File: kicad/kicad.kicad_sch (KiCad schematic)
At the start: 7 parts, among them J1 Screw_Terminal_01x14, U1 Pico

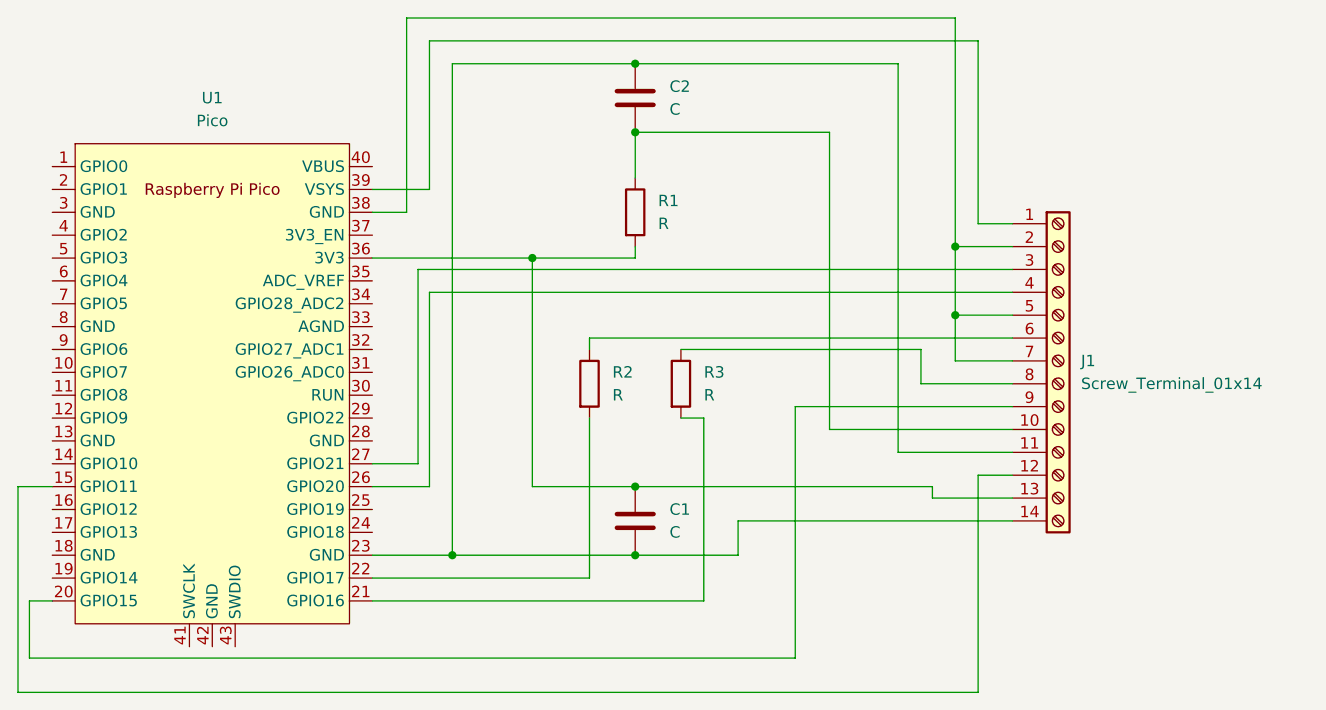
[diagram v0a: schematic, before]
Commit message: added kicad board that I'm getting printed
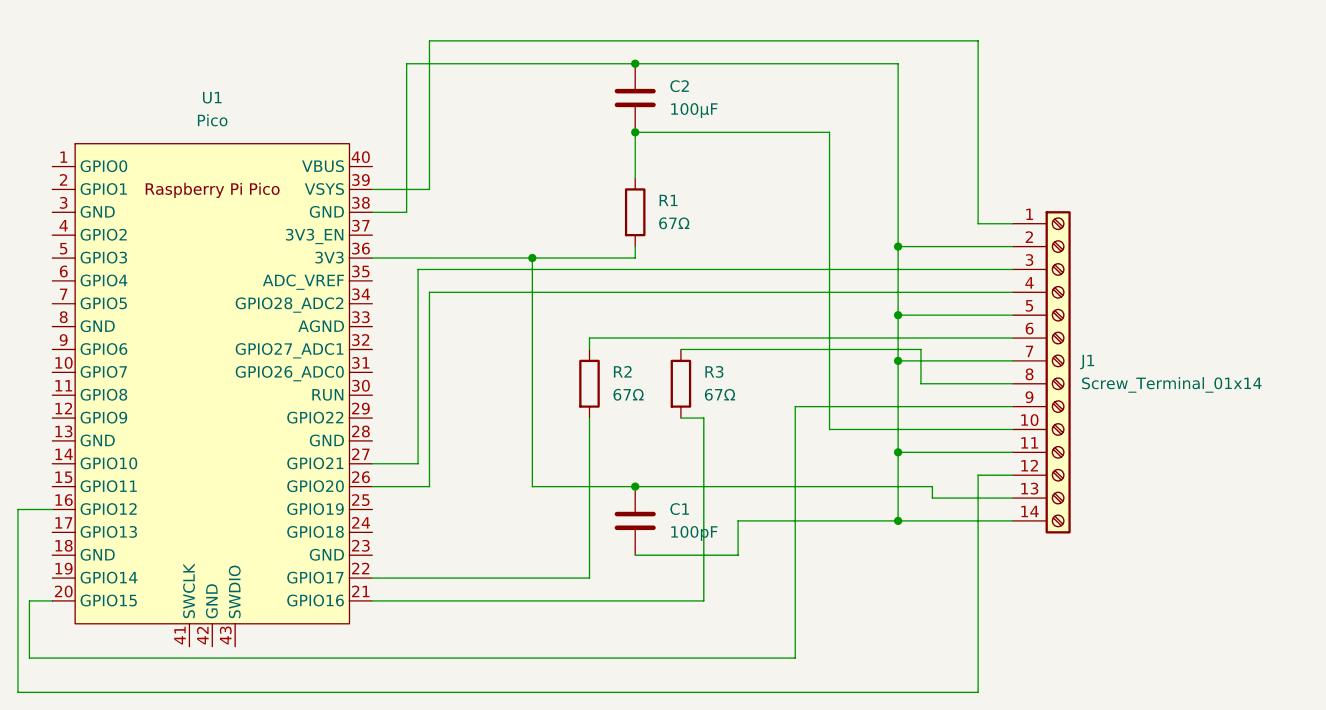
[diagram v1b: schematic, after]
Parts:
- C1: value C -> 100pF; footprint Capacitor_SMD:C_Elec_3x5.4 -> Capacitor_THT:C_Disc_D7.0mm_W2.5mm_P5.00mm
- C2: value C -> 100μF; footprint Capacitor_SMD:C_Elec_3x5.4 -> Capacitor_THT:C_Disc_D7.0mm_W2.5mm_P5.00mm
- J1: footprint (none) -> Library:terminal_block_14
- R1, R2, R3: value R -> 67Ω; footprint (none) -> Resistor_THT:R_Axial_DIN0207_L6.3mm_D2.5mm_P10.16mm_Horizontal
- U1: footprint RPi_Pico:RPi_Pico_SMD_TH -> MCU_RaspberryPi_and_Boards:RPi_Pico_SMD_TH
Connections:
- net at C1.2, C2.1, J1.11 (Pin_11)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: now also J1.2 (Pin_2), J1.5 (Pin_5), J1.7 (Pin_7), U1.38 (GND); no longer U1.23 (GND)
- net at U1.15 (GPIO11): no longer J1.12 (Pin_12)
- net at U1.16 (GPIO12): now also J1.12 (Pin_12)
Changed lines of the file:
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@@
 (kicad_sch (version 20230121) (generator eeschema)
   (paper "A4")
+  (junction (at 217.17 88.9) (diameter 0) (color 0 0 0 0)
+  )
+  (junction (at 217.17 106.68) (diameter 0) (color 0 0 0 0)
+  )
+  (junction (at 217.17 83.82) (diameter 0) (color 0 0 0 0)
+  )
   (junction (at 176.53 77.47) (diameter 0) (color 0 0 0 0)
   )
-  (junction (at 167.64 110.49) (diameter 0) (color 0 0 0 0)
+  (junction (at 217.17 99.06) (diameter 0) (color 0 0 0 0)
   )
   (junction (at 187.96 55.88) (diameter 0) (color 0 0 0 0)
   )
-  (junction (at 223.52 76.2) (diameter 0) (color 0 0 0 0)
-  )
-  (junction (at 187.96 110.49) (diameter 0) (color 0 0 0 0)
-  )
   (junction (at 187.96 102.87) (diameter 0) (color 0 0 0 0)
   )
-  (junction (at 223.52 83.82) (diameter 0) (color 0 0 0 0)
+  (junction (at 217.17 76.2) (diameter 0) (color 0 0 0 0)
   )
   (junction (at 187.96 63.5) (diameter 0) (color 0 0 0 0)
@@
     (stroke (width 0) (type default))
   )
+  (wire (pts (xy 119.38 105.41) (xy 123.19 105.41))
+    (stroke (width 0) (type default))
+  )
   (wire (pts (xy 187.96 63.5) (xy 209.55 63.5))
     (stroke (width 0) (type default))
@@
     (stroke (width 0) (type default))
   )
-  (wire (pts (xy 223.52 88.9) (xy 229.87 88.9))
+  (wire (pts (xy 217.17 88.9) (xy 229.87 88.9))
     (stroke (width 0) (type default))
   )
@@
     (stroke (width 0) (type default))
   )
-  (wire (pts (xy 167.64 55.88) (xy 187.96 55.88))
-    (stroke (width 0) (type default))
-  )
-  (wire (pts (xy 223.52 76.2) (xy 229.87 76.2))
-    (stroke (width 0) (type default))
-  )
-  (wire (pts (xy 223.52 83.82) (xy 229.87 83.82))
-    (stroke (width 0) (type default))
-  )
-  (wire (pts (xy 162.56 50.8) (xy 223.52 50.8))
+  (wire (pts (xy 162.56 55.88) (xy 187.96 55.88))
+    (stroke (width 0) (type default))
+  )
+  (wire (pts (xy 217.17 76.2) (xy 229.87 76.2))
+    (stroke (width 0) (type default))
+  )
+  (wire (pts (xy 217.17 83.82) (xy 229.87 83.82))
     (stroke (width 0) (type default))
   )
@@
     (stroke (width 0) (type default))
   )
+  (wire (pts (xy 217.17 99.06) (xy 217.17 106.68))
+    (stroke (width 0) (type default))
+  )
   (wire (pts (xy 176.53 102.87) (xy 187.96 102.87))
     (stroke (width 0) (type default))
@@
     (stroke (width 0) (type default))
   )
+  (wire (pts (xy 217.17 83.82) (xy 217.17 88.9))
+    (stroke (width 0) (type default))
+  )
   (wire (pts (xy 205.74 93.98) (xy 229.87 93.98))
     (stroke (width 0) (type default))
@@
     (stroke (width 0) (type default))
   )
+  (wire (pts (xy 119.38 125.73) (xy 119.38 105.41))
+    (stroke (width 0) (type default))
+  )
   (wire (pts (xy 176.53 77.47) (xy 187.96 77.47))
     (stroke (width 0) (type default))
@@
     (stroke (width 0) (type default))
   )
-  (wire (pts (xy 223.52 76.2) (xy 223.52 83.82))
-    (stroke (width 0) (type default))
-  )
-  (wire (pts (xy 229.87 106.68) (xy 199.39 106.68))
+  (wire (pts (xy 229.87 106.68) (xy 217.17 106.68))
     (stroke (width 0) (type default))
   )
@@
     (stroke (width 0) (type default))
   )
-  (wire (pts (xy 162.56 72.39) (xy 162.56 50.8))
+  (wire (pts (xy 162.56 72.39) (xy 162.56 55.88))
     (stroke (width 0) (type default))
   )
@@
     (stroke (width 0) (type default))
   )
+  (wire (pts (xy 217.17 88.9) (xy 217.17 99.06))
+    (stroke (width 0) (type default))
+  )
   (wire (pts (xy 209.55 96.52) (xy 229.87 96.52))
     (stroke (width 0) (type default))
   )
-  (wire (pts (xy 167.64 110.49) (xy 187.96 110.49))
-    (stroke (width 0) (type default))
-  )
   (wire (pts (xy 165.1 81.28) (xy 229.87 81.28))
     (stroke (width 0) (type default))
   )
-  (wire (pts (xy 123.19 102.87) (xy 119.38 102.87))
-    (stroke (width 0) (type default))
-  )
   (wire (pts (xy 119.38 125.73) (xy 226.06 125.73))
     (stroke (width 0) (type default))
@@
     (stroke (width 0) (type default))
   )
-  (wire (pts (xy 223.52 50.8) (xy 223.52 76.2))
-    (stroke (width 0) (type default))
-  )
   (wire (pts (xy 195.58 115.57) (xy 195.58 95.25))
     (stroke (width 0) (type default))
   )
+  (wire (pts (xy 217.17 106.68) (xy 199.39 106.68))
+    (stroke (width 0) (type default))
+  )
   (wire (pts (xy 209.55 63.5) (xy 209.55 96.52))
     (stroke (width 0) (type default))
   )
-  (wire (pts (xy 217.17 55.88) (xy 217.17 99.06))
+  (wire (pts (xy 217.17 55.88) (xy 217.17 76.2))
     (stroke (width 0) (type default))
   )
@@
     (stroke (width 0) (type default))
   )
-  (wire (pts (xy 119.38 102.87) (xy 119.38 125.73))
-    (stroke (width 0) (type default))
-  )
   (wire (pts (xy 120.65 115.57) (xy 120.65 121.92))
     (stroke (width 0) (type default))
@@
     (stroke (width 0) (type default))
   )
-  (wire (pts (xy 158.75 110.49) (xy 167.64 110.49))
-    (stroke (width 0) (type default))
-  )
   (wire (pts (xy 226.06 125.73) (xy 226.06 101.6))
     (stroke (width 0) (type default))
@@
     (stroke (width 0) (type default))
   )
+  (wire (pts (xy 217.17 76.2) (xy 217.17 83.82))
+    (stroke (width 0) (type default))
+  )
   (wire (pts (xy 158.75 72.39) (xy 162.56 72.39))
     (stroke (width 0) (type default))
   )
-  (wire (pts (xy 223.52 83.82) (xy 223.52 88.9))
-    (stroke (width 0) (type default))
-  )
-  (wire (pts (xy 167.64 110.49) (xy 167.64 55.88))
-    (stroke (width 0) (type default))
-  )
   (symbol (lib_id "Device:R") (at 193.04 91.44 0) (unit 1)
     (in_bom yes) (on_board yes) (dnp no) (fields_autoplaced)
@@
       (effects (font (size 1.27 1.27)) (justify left))
     )
-    (property "Value" "R" (at 195.58 92.71 0)
-      (effects (font (size 1.27 1.27)) (justify left))
-    )
-    (property "Footprint" "" (at 191.262 91.44 90)
+    (property "Value" "67Ω" (at 195.58 92.71 0)
+      (effects (font (size 1.27 1.27)) (justify left))
+    )
+    (property "Footprint" "Resistor_THT:R_Axial_DIN0207_L6.3mm_D2.5mm_P10.16mm_Horizontal" (at 191.262 91.44 90)
       (effects (font (size 1.27 1.27)) hide)
     )
@@
       (effects (font (size 1.27 1.27)) (justify left))
     )
-    (property "Value" "R" (at 185.42 92.71 0)
-      (effects (font (size 1.27 1.27)) (justify left))
-    )
-    (property "Footprint" "" (at 181.102 91.44 90)
+    (property "Value" "67Ω" (at 185.42 92.71 0)
+      (effects (font (size 1.27 1.27)) (justify left))
+    )
+    (property "Footprint" "Resistor_THT:R_Axial_DIN0207_L6.3mm_D2.5mm_P10.16mm_Horizontal" (at 181.102 91.44 90)
       (effects (font (size 1.27 1.27)) hide)
     )
@@
       (effects (font (size 1.27 1.27)) (justify left))
     )
-    (property "Value" "R" (at 190.5 73.66 0)
-      (effects (font (size 1.27 1.27)) (justify left))
-    )
-    (property "Footprint" "" (at 186.182 72.39 90)
+    (property "Value" "67Ω" (at 190.5 73.66 0)
+      (effects (font (size 1.27 1.27)) (justify left))
+    )
+    (property "Footprint" "Resistor_THT:R_Axial_DIN0207_L6.3mm_D2.5mm_P10.16mm_Horizontal" (at 186.182 72.39 90)
       (effects (font (size 1.27 1.27)) hide)
     )
@@
       (effects (font (size 1.27 1.27)) (justify left))
     )
-    (property "Value" "C" (at 191.77 107.95 0)
-      (effects (font (size 1.27 1.27)) (justify left))
-    )
-    (property "Footprint" "Capacitor_SMD:C_Elec_3x5.4" (at 188.9252 110.49 0)
+    (property "Value" "100pF" (at 191.77 107.95 0)
+      (effects (font (size 1.27 1.27)) (justify left))
+    )
+    (property "Footprint" "Capacitor_THT:C_Disc_D7.0mm_W2.5mm_P5.00mm" (at 188.9252 110.49 0)
       (effects (font (size 1.27 1.27)) hide)
     )
@@
       (effects (font (size 1.27 1.27)))
     )
-    (property "Footprint" "RPi_Pico:RPi_Pico_SMD_TH" (at 140.97 91.44 90)
+    (property "Footprint" "MCU_RaspberryPi_and_Boards:RPi_Pico_SMD_TH" (at 140.97 91.44 90)
       (effects (font (size 1.27 1.27)) hide)
     )
@@
       (effects (font (size 1.27 1.27)) hide)
     )
-    (pin "43")
-    (pin "24")
-    (pin "40")
+    (pin "6")
+    (pin "2")
     (pin "3")
     (pin "38")
+    (pin "41")
+    (pin "28")
+    (pin "5")
+    (pin "37")
+    (pin "34")
+    (pin "26")
+    (pin "32")
+    (pin "35")
+    (pin "9")
+    (pin "25")
+    (pin "39")
+    (pin "18")
+    (pin "17")
+    (pin "36")
+    (pin "43")
+    (pin "31")
+    (pin "23")
+    (pin "42")
+    (pin "8")
+    (pin "40")
+    (pin "11")
+    (pin "15")
+    (pin "30")
+    (pin "24")
+    (pin "33")
+    (pin "29")
+    (pin "19")
     (pin "7")
     (pin "27")
+    (pin "4")
+    (pin "12")
+    (pin "14")
     (pin "21")
+    (pin "20")
+    (pin "10")
+    (pin "13")
+    (pin "1")
     (pin "22")
-    (pin "42")
-    (pin "4")
-    (pin "31")
-    (pin "26")
-    (pin "12")
-    (pin "15")
-    (pin "13")
-    (pin "14")
-    (pin "20")
-    (pin "9")
     (pin "16")
-    (pin "19")
-    (pin "39")
-    (pin "17")
-    (pin "32")
-    (pin "34")
-    (pin "33")
-    (pin "2")
-    (pin "29")
-    (pin "8")
-    (pin "28")
-    (pin "37")
-    (pin "30")
-    (pin "5")
-    (pin "6")
-    (pin "23")
-    (pin "35")
-    (pin "25")
-    (pin "18")
-    (pin "10")
-    (pin "11")
-    (pin "1")
-    (pin "36")
-    (pin "41")
     (instances
       (project "kicad"
@@
       (effects (font (size 1.27 1.27)) (justify left))
     )
-    (property "Value" "C" (at 191.77 60.96 0)
-      (effects (font (size 1.27 1.27)) (justify left))
-    )
-    (property "Footprint" "Capacitor_SMD:C_Elec_3x5.4" (at 188.9252 63.5 0)
+    (property "Value" "100μF" (at 191.77 60.96 0)
+      (effects (font (size 1.27 1.27)) (justify left))
+    )
+    (property "Footprint" "Capacitor_THT:C_Disc_D7.0mm_W2.5mm_P5.00mm" (at 188.9252 63.5 0)
       (effects (font (size 1.27 1.27)) hide)
     )
@@
       (effects (font (size 1.27 1.27)) (justify left))
     )
-    (property "Footprint" "" (at 234.95 88.9 0)
-      (effects (font (size 1.27 1.27)) hide)
-    )
+    (property "Footprint" "Library:terminal_block_14" (at 234.95 88.9 0)
+      (effects (font (size 1.27 1.27)) hide)
+    )
